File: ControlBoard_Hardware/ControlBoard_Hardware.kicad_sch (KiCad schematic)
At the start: 27 parts, among them U2 TSR_1-2450

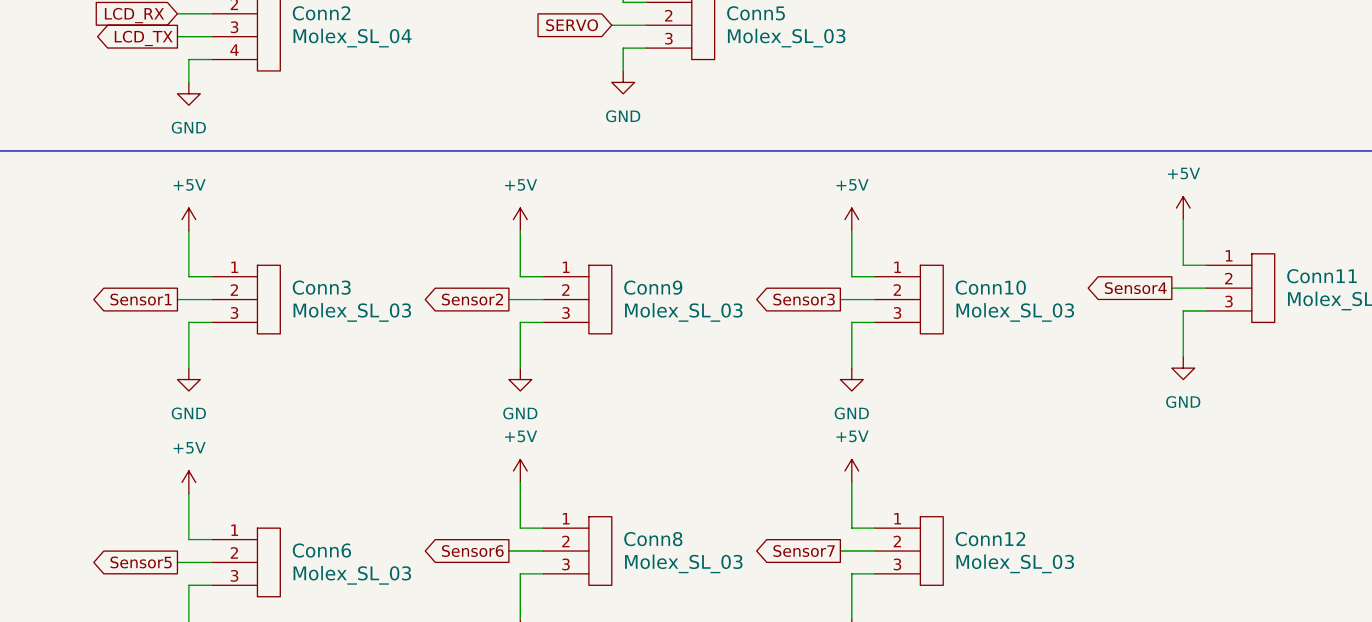
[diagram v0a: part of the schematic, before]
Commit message: fixed voltage level on coil sensors
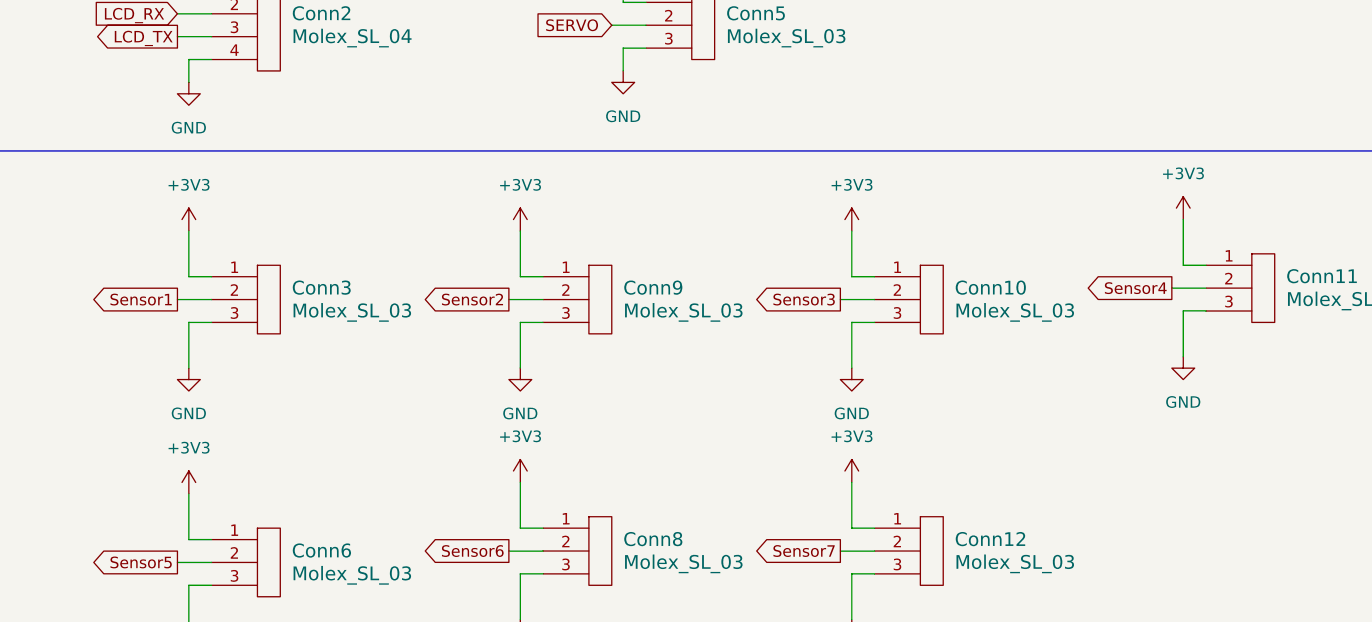
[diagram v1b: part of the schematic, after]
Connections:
- net +3V3: now also Conn10.1, Conn11.1, Conn12.1, Conn3.1, Conn6.1, Conn8.1, Conn9.1
- net +5V: no longer Conn10.1, Conn11.1, Conn12.1, Conn3.1, Conn6.1, Conn8.1, Conn9.1

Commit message: Updated schematic
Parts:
- removed Conn10, Conn11, Conn12, Conn3, Conn6, Conn8, Conn9: Molex_SL_03, MRDT_Connectors:MOLEX_SL_03_Horizontal, symbol MRDT_Connectors:Molex_SL_03
- removed D3: LED, LED_SMD:LED_0603_1608Metric_Pad1.05x0.95mm_HandSolder, symbol Device:LED
- removed R3: 100, Resistor_SMD:R_0603_1608Metric_Pad0.98x0.95mm_HandSolder, symbol Device:R
- added Conn10, Conn11, Conn3, Conn6, Conn8, Conn9: Molex_SL_02, MRDT_Connectors:MOLEX_SL_02_Horizontal, symbol MRDT_Connectors:Molex_SL_02
- added J1: Conn_01x03, symbol Connector_Generic:Conn_01x03
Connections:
- net +3V3 is gone; now on net GND: U1. (Vin)
- net +5V: now also J1.1 (Pin_1)
- net GND: now also Conn10.2, Conn11.2, Conn3.2, Conn6.2, Conn8.2, Conn9.2, J1.3 (Pin_3)
- net Sensor1: no longer names the net of U1.17 (A3)
- net Sensor2 renamed Coil6
- net Coil6: now also Conn11.1
- net Sensor3 renamed Coil5
- net Coil5: now also Conn10.1
- net Sensor4 renamed Coil4
- net Coil4: now also Conn9.1
- net Sensor5 renamed Coil3
- net Coil3: now also Conn8.1
- net Sensor6 renamed Coil2
- net Coil2: now also Conn6.1
- net Sensor7 renamed Coil1
- net Coil1: now also Conn3.1
- new net LED Data: J1.2 (Pin_2)
- no-connect marks 11 -> 12
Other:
- note removed: "Optical Sensors"

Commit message: updated schematic
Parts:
- removed J1: Conn_01x03, symbol Connector_Generic:Conn_01x03
- added Conn12: Molex_SL_03, MRDT_Connectors:MOLEX_SL_03_Horizontal, symbol MRDT_Connectors:Molex_SL_03
- H1, H2, H3, H4: footprint MRDT_Drill_Holes:4_40_Hole_Corner -> MountingHole:MountingHole_3.2mm_M3
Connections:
- net +5V: now also Conn12.1
- net GND: now also Conn12.3
- net LED Data: now also Conn12.2
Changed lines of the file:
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@@
     (stroke (width 0) (type default))
   )
-  (wire (pts (xy 189.23 90.17) (xy 187.96 90.17))
+  (wire (pts (xy 187.96 90.17) (xy 191.77 90.17))
     (stroke (width 0) (type default))
   )
@@
     (stroke (width 0) (type default))
   )
+  (wire (pts (xy 189.23 87.63) (xy 191.77 87.63))
+    (stroke (width 0) (type default))
+  )
   (wire (pts (xy 55.88 123.19) (xy 60.96 123.19))
     (stroke (width 0) (type default))
@@
     (stroke (width 0) (type default))
   )
-  (wire (pts (xy 189.23 85.09) (xy 187.96 85.09))
+  (wire (pts (xy 187.96 85.09) (xy 191.77 85.09))
     (stroke (width 0) (type default))
   )
@@
       (effects (font (size 1.27 1.27)) (justify left))
     )
-    (property "Footprint" "MRDT_Drill_Holes:4_40_Hole_Corner" (at 65.0376 179.0699 0)
+    (property "Footprint" "MountingHole:MountingHole_3.2mm_M3" (at 65.0376 179.0699 0)
       (effects (font (size 1.27 1.27)) hide)
     )
@@
       (effects (font (size 1.27 1.27)) (justify left))
     )
-    (property "Footprint" "MRDT_Drill_Holes:4_40_Hole_Corner" (at 25.4 179.07 0)
+    (property "Footprint" "MountingHole:MountingHole_3.2mm_M3" (at 25.4 179.07 0)
       (effects (font (size 1.27 1.27)) hide)
     )
@@
       (effects (font (size 1.27 1.27)) (justify left))
     )
-    (property "Footprint" "MRDT_Drill_Holes:4_40_Hole_Corner" (at 45.72 179.07 0)
+    (property "Footprint" "MountingHole:MountingHole_3.2mm_M3" (at 45.72 179.07 0)
       (effects (font (size 1.27 1.27)) hide)
     )
@@
     )
   )
-  (symbol (lib_id "Connector_Generic:Conn_01x03") (at 194.31 87.63 0) (unit 1)
-    (in_bom yes) (on_board yes) (dnp no) (fields_autoplaced)
-    (property "Reference" "J1" (at 196.85 86.36 0)
-      (effects (font (size 1.27 1.27)) (justify left))
-    )
-    (property "Value" "Conn_01x03" (at 196.85 88.9 0)
-      (effects (font (size 1.27 1.27)) (justify left))
-    )
-    (property "Footprint" "" (at 194.31 87.63 0)
-      (effects (font (size 1.27 1.27)) hide)
-    )
-    (property "Datasheet" "~" (at 194.31 87.63 0)
-      (effects (font (size 1.27 1.27)) hide)
-    )
-    (pin "1")
-    (pin "2")
-    (pin "3")
-    (instances
-      (project "ControlBoard_Hardware"
-        (path "/487df2d1-0681-470c-8e27-af1d48fa6afe"
-          (reference "J1") (unit 1)
-        )
-      )
-    )
-  )
   (symbol (lib_id "Device:R") (at 67.31 35.56 0) (unit 1)
     (in_bom yes) (on_board yes) (dnp no) (fields_autoplaced)
@@
       (effects (font (size 1.27 1.27)) (justify left))
     )
-    (property "Footprint" "MRDT_Drill_Holes:4_40_Hole_Corner" (at 85.09 179.07 0)
+    (property "Footprint" "MountingHole:MountingHole_3.2mm_M3" (at 85.09 179.07 0)
       (effects (font (size 1.27 1.27)) hide)
     )
@@
         )
       )
+    )
+  )
+  (symbol (lib_id "MRDT_Connectors:Molex_SL_03") (at 196.85 91.44 0) (unit 1)
+    (in_bom yes) (on_board yes) (dnp no) (fields_autoplaced)
+    (property "Reference" "Conn12" (at 200.66 86.36 0)
+      (effects (font (size 1.524 1.524)) (justify left))
+    )
+    (property "Value" "Molex_SL_03" (at 200.66 88.9 0)
+      (effects (font (size 1.524 1.524)) (justify left))
+    )
+    (property "Footprint" "MRDT_Connectors:MOLEX_SL_03_Horizontal" (at 196.85 91.44 0)
+      (effects (font (size 1.524 1.524)) hide)
+    )
+    (property "Datasheet" "" (at 196.85 91.44 0)
+      (effects (font (size 1.524 1.524)) hide)
+    )
+    (pin "1")
+    (pin "2")
+    (pin "3")
+    (instances
+      (project "ControlBoard_Hardware"
+        (path "/487df2d1-0681-470c-8e27-af1d48fa6afe"
+          (reference "Conn12") (unit 1)
+        )
+      )

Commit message: sus gate driver
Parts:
- added U3: ~, Package_LCC:PLCC-44_THT-Socket, symbol GateDriver:IR2131J
- Conn1: footprint MRDT_Connectors:MOLEX_SL_02_Horizontal -> Package_LCC:PLCC-44
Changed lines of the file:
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@@
+    )
+  )
+  (symbol (lib_id "GateDriver:IR2131J") (at 256.54 72.39 0) (unit 1)
+    (in_bom yes) (on_board yes) (dnp no) (fields_autoplaced)
+    (property "Reference" "U3" (at 273.05 70.5419 0)
+      (effects (font (size 1.27 1.27)))
+    )
+    (property "Value" "~" (at 256.54 72.39 0)
+      (effects (font (size 1.27 1.27)))
+    )
+    (property "Footprint" "Package_LCC:PLCC-44_THT-Socket" (at 256.54 72.39 0)
+      (effects (font (size 1.27 1.27)) hide)
+    )
+    (property "Datasheet" "" (at 256.54 72.39 0)
+      (effects (font (size 1.27 1.27)) hide)
+    )
+    (pin "10")
+    (pin "11")
+    (pin "12")
+    (pin "13")
+    (pin "14")
+    (pin "15")
+    (pin "16")
+    (pin "17")
+    (pin "18")
+    (pin "19")
+    (pin "20")
+    (pin "21")
+    (pin "22")
+    (pin "23")
+    (pin "24")
+    (pin "25")
+    (pin "29")
+    (pin "3")
+    (pin "30")
+    (pin "31")
+    (pin "35")
+    (pin "36")
+    (pin "37")
+    (pin "4")
+    (pin "41")
+    (pin "42")
+    (pin "43")
+    (pin "5")
+    (pin "6")
+    (pin "7")
+    (pin "8")
+    (pin "9")
+    (instances
+      (project "ControlBoard_Hardware"
+        (path "/487df2d1-0681-470c-8e27-af1d48fa6afe"
+          (reference "U3") (unit 1)
+        )
+      )
     )
   )
@@
       (effects (font (size 1.524 1.524)))
     )
-    (property "Footprint" "MRDT_Connectors:MOLEX_SL_02_Horizontal" (at 22.86 20.32 0)
+    (property "Footprint" "Package_LCC:PLCC-44" (at 22.86 20.32 0)
       (effects (font (size 1.524 1.524)) hide)
     )

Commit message: updated schematic
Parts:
- removed Conn3, Conn4: Molex_SL_02, MRDT_Connectors:MOLEX_SL_02_Horizontal, symbol MRDT_Connectors:Molex_SL_02
- removed U3: ~, Package_LCC:PLCC-44_THT-Socket, symbol GateDriver:IR2131J
- added C1: 1000uF, https://www.mouser.com/datasheet/2/447/KEM_A4004_ESK-3316395.pdf, symbol Device:C
- added C10, C12, C2, C4, C6, C8: 10uF, symbol Device:C_Small
- added C11, C13, C3, C5, C7, C9: 0.1uF, symbol Device:C_Small
- added Conn3: Molex_SL_05, symbol MRDT_Connectors:Molex_SL_05
- added Conn4: Molex_SL_04, MRDT_Connectors:MOLEX_SL_04_Horizontal, symbol MRDT_Connectors:Molex_SL_04
- added D3, D4: LED, LED_SMD:LED_0603_1608Metric_Pad1.05x0.95mm_HandSolder, symbol Device:LED
- added R3: 1000, Resistor_SMD:R_0603_1608Metric_Pad0.98x0.95mm_HandSolder, symbol Device:R
- added R4: 120, Resistor_SMD:R_0603_1608Metric_Pad0.98x0.95mm_HandSolder, symbol Device:R
- added R5: 300, symbol Device:R
- added U10, U3, U6, U7, U8, U9: MCP1415, Package_TO_SOT_SMD:SOT-23-5, symbol Driver_FET:MCP1415
- added U11: TSR_1-2450, Converter_DCDC:Converter_DCDC_TRACO_TSR-1_THT, symbol Regulator_Switching:TSR_1-2450
- added U4: OKI-78SR-12_1.0-W36H-C, Converter_DCDC:Converter_DCDC_Murata_OKI-78SR_Horizontal, symbol Converter_DCDC:OKI-78SR-12_1.0-W36H-C
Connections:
- net +5V: no longer Conn12.1
- net GND: now also C1.2, C10.2, C11.2, C12.2, C13.2, C2.2, C3.2, C4.2, C5.2, C6.2, C7.2, C8.2, C9.2, Conn3.5, Conn4.4, D3.1 (K), D4.1 (K), U10.4 (GND), U11.2 (GND), U3.4 (GND), U4.2 (GND), U6.4 (GND), U7.4 (GND), U8.4 (GND), U9.4 (GND)
- net Input_PWR: now also U11.1 (Vin), U4.1 (IN)
- net LCD_RX: now also U1.0 (RX1); no longer U1.1 (TX1)
- net LCD_TX: now also U1.1 (TX1); no longer U1.0 (RX1)
- net LED Data: now also U1.7 (RX2), C1.1, R5.1; no longer Conn12.2
- net SERVO: no longer U1.6 (OUT1D)
- net Trigger Signal: no longer U1.12 (MISO)
- net Voltage_Sens: now reaches U1.10 (CS)
- net Voltage_Sens: now also Conn3.2
- net Relay_Toggle: now reaches U1.11 (MOSI)
- net Relay_Toggle: now also Conn3.3
- net COIL_6_L: now reaches U1.17 (A3)
- net COIL_6_L: now also U10.3 (IN)
- net Charge_Toggle: now reaches U1.2 (OUT2)
- net Charge_Toggle: now also Conn4.1
- net FAULT: now reaches U1.3 (LRCLK2)
- net FAULT: now also Conn4.2
- net DONE: now reaches U1.4 (BCLK2)
- net DONE: now also Conn4.3
- net Charge: no longer names the net of U1.13 (SCK)
- net Coil1: no longer names the net of U1.23 (A9)
- net Coil2 renamed COIL_1_L
- net COIL_1_L: now also U3.3 (IN); no longer Conn6.1
- net Coil3 renamed COIL_2_L
- net COIL_2_L: now also U6.3 (IN); no longer Conn8.1
- net Coil4 renamed COIL_3_L
- net COIL_3_L: now also U7.3 (IN); no longer Conn9.1
- net Coil5 renamed COIL_4_L
- net COIL_4_L: now also U9.3 (IN); no longer Conn10.1
- net Coil6 renamed COIL_5_L
- net COIL_5_L: now also U8.3 (IN); no longer Conn11.1
- net Discharge: no longer names the net of U1.5 (IN2)
- net Discharge: no longer Conn14.1
- new net: D3.2 (A), R3.2
- new net: D4.2 (A), R4.2
- new net: Conn12.2, R5.2
- new net +12V: C10.1, C11.1, C12.1, C13.1, C2.1, C3.1, C4.1, C5.1, C6.1, C7.1, C8.1, C9.1, R3.1, U10.2 (Vdd), U3.2 (Vdd), U4.3 (OUT), U6.2 (Vdd), U7.2 (Vdd), U8.2 (Vdd), U9.2 (Vdd)
- new net +3.3V: Conn3.1, R4.1
- new net +5VA: Conn12.1, U11.3 (Vout)
- new net COIL_1_T: Conn6.1, U3.5 (~{OUT})
- new net COIL_2_T: Conn8.1, U6.5 (~{OUT})
- new net COIL_3_T: Conn9.1, U7.5 (~{OUT})
- new net COIL_4_T: Conn10.1, U9.5 (~{OUT})
- new net COIL_5_T: Conn11.1, U8.5 (~{OUT})
- new net COIL_6_T: Conn14.1, U10.5 (~{OUT})
- new net Discharge_Toggle: Conn3.4, U1.12 (MISO)
- no-connect marks 12 -> 0
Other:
- note removed: "Charging/Discharging Circuits"
- note removed: "LCD"
- note removed: "Power"
- note removed: "Safety Switch"
- note removed: "Teensy"
- note removed: "Trigger"
- moved on the sheet: Conn1, D1, D2, H1, H2, H3, H4, PowerSwich1, R1, R2, U2

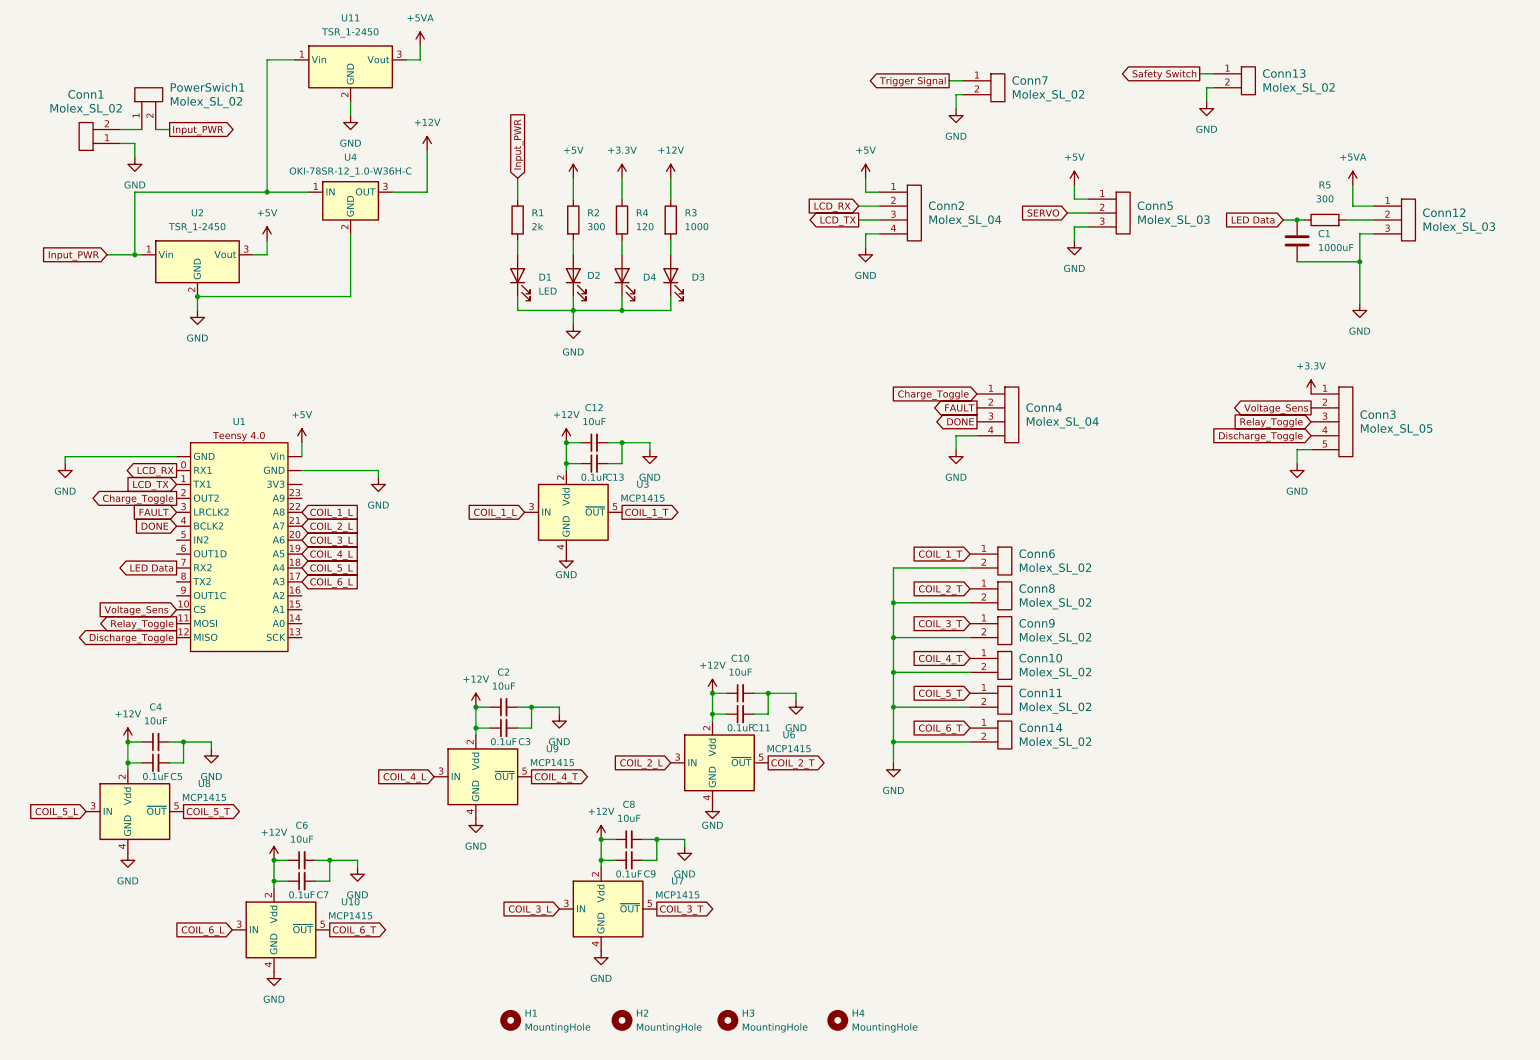
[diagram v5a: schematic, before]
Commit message: Started layout
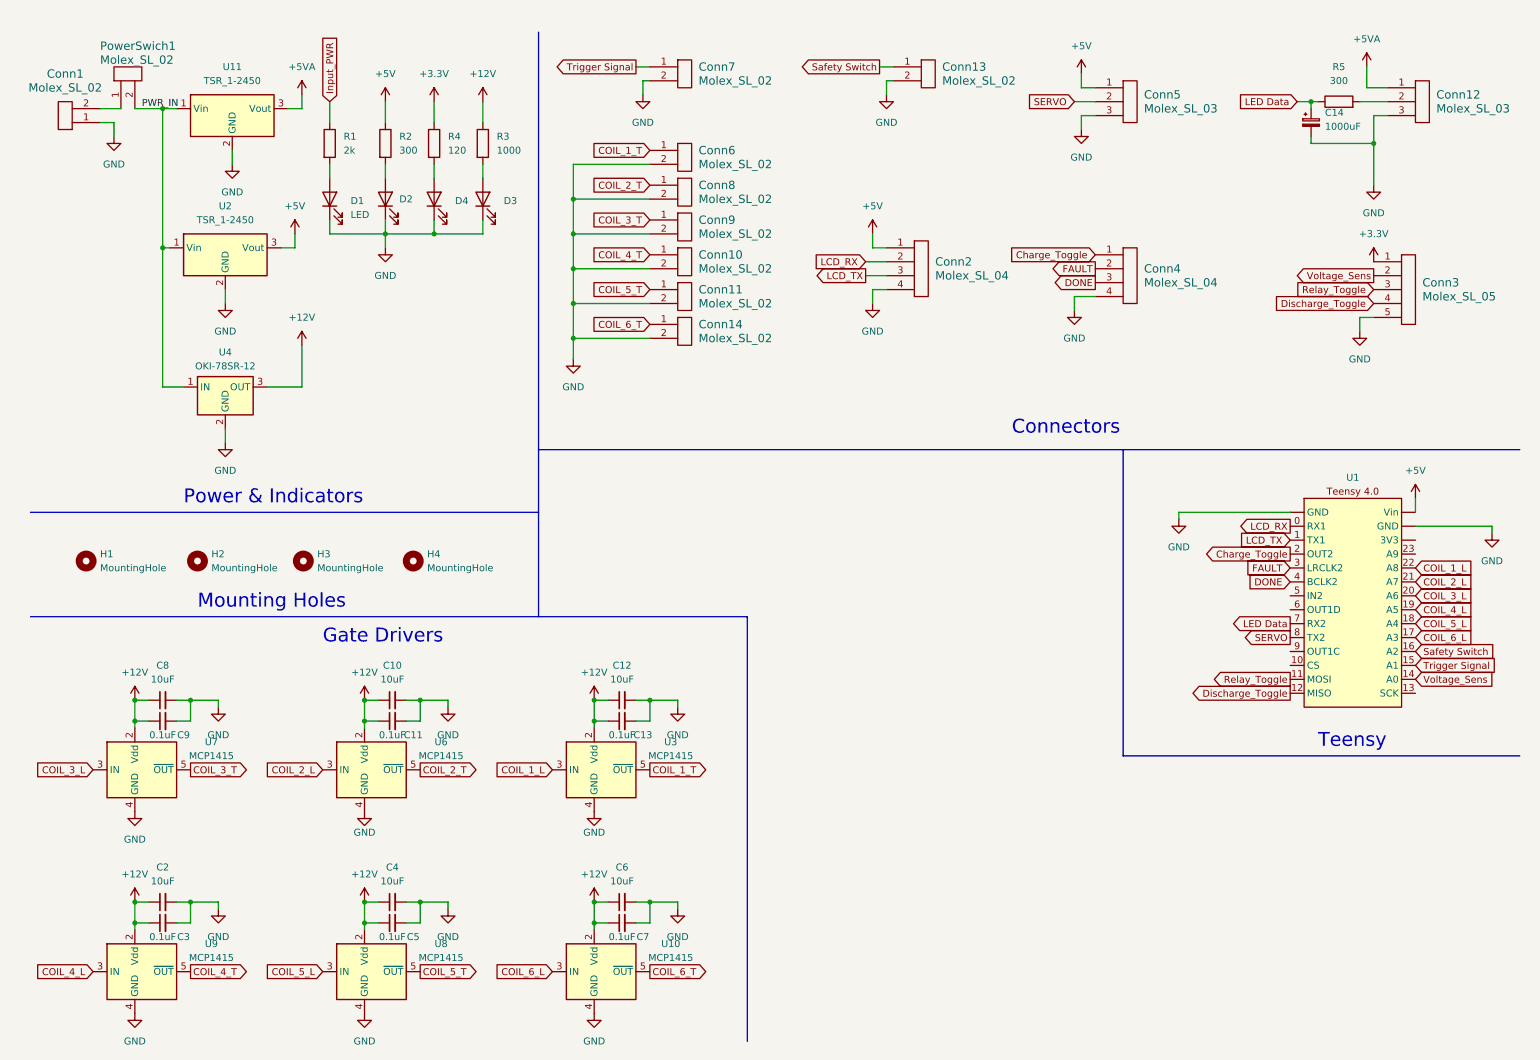
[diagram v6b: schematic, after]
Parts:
- removed C1: 1000uF, https://www.mouser.com/datasheet/2/447/KEM_A4004_ESK-3316395.pdf, symbol Device:C
- added C14: 1000uF, Capacitor_THT:CP_Radial_D8.0mm_P3.50mm, symbol Device:C_Polarized_Small
- C10, C11, C12, C13, C2, C3, C4, C5, C6, C7, C8, C9: footprint (none) -> Capacitor_SMD:C_0603_1608Metric_Pad1.08x0.95mm_HandSolder
- Conn1: footprint Package_LCC:PLCC-44 -> MRDT_Connectors:MOLEX_SL_02_Horizontal
- Conn3: footprint (none) -> MRDT_Connectors:MOLEX_SL_05_Horizontal
- R5: footprint (none) -> Resistor_SMD:R_0603_1608Metric_Pad0.98x0.95mm_HandSolder
- U4: value OKI-78SR-12_1.0-W36H-C -> OKI-78SR-12
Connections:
- net GND: now also C14.2
- net Input_PWR: no longer PowerSwich1.2, U11.1 (Vin), U2.1 (Vin), U4.1 (IN)
- net LED Data: now also C14.1
- net SERVO: now also U1.8 (TX2)
- net Safety Switch: now also U1.16 (A2)
- net Trigger Signal: now also U1.15 (A1)
- net Voltage_Sens: now also U1.14 (A0); no longer U1.10 (CS)
- new net PWR_IN: PowerSwich1.2, U11.1 (Vin), U2.1 (Vin), U4.1 (IN)
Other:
- note added: "Connectors"
- note added: "Gate Drivers"
- note added: "Mounting Holes"
- note added: "Power & Indicators"
- note added: "Teensy"
- moved on the sheet: C10, C11, C12, C13, C2, C3, C4, C5, C6, C7, C8, C9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
